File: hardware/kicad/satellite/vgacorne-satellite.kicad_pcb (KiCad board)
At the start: 2 copper layers, 134.4 x 93.5 mm, 110 parts, among them J3 SM10B-SRSS-TB, SW1 C0R0, SW10 C3R0, SW11 C3R1, SW12 C3R2, SW13 C4R0, SW14 C4R1, SW15 C4R2, SW16 C5R0, SW17 C5R1, SW18 C5R2, SW19 T0, SW2 C0R1, SW20 T1, SW21 T2, SW3 C0R2, SW4 C1R0, SW5 C1R1, SW6 C1R2, SW7 C2R0, SW8 C2R1, SW9 C2R2, U11 SN74LV4051APWR, U12 SN74LV4051APWR, U13 SN74LV4051APWR, U2 TLV75733PDBVR, U5 TLV9064IPWR, U6 SRV05-4, U7 SRV05-4

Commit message: Add trackpad, mouse column and scroll wheel; move MCU and ports
Layout
- MCU module, USB-C and trackpad move to the right half; the left half
  is now the passive satellite.
- VGA daughterboard bay moves to the inner-back corner so both cables
  leave from the back face. The bay sits 4.5 mm further back than the
  keys need, so both halves are 116 mm deep.
- Azoteq TPS65 trackpad, landscape, right beside Y/H/N under a 1 mm
  overlay. The MCU module moves to a PCB ear behind it, next to the
  VGA bay. trackpad.py selects the pad (TPS65 or 40 mm Cirque); the
  case pocket, J5 connector and QMK driver follow the selection.
- Left half: a mouse column beside T/G/B with a scroll wheel (Bourns
  PEC12R) at the top and left/right-click HE keys beside G and B.

Circuits and firmware
- Mux channels reassigned so the satellite's mouse keys and wheel fill
  its three spare channels. The wheel's A/B contacts are summed into
  four voltage levels on one channel.
- QMK: 44-key LAYOUT and a wheel decoder that feeds QMK's quadrature
  encoder driver. Trackpad on I2C1, with rules.mk now generated. The
  host test covers the wheel.
- libhmk: MS_BTN1/MS_BTN2 on the mouse keys (no encoder support).

Case and renders
- Smoother milled case: 7.25 mm walls, 25 mm minimum outside radius
  and a flat back face at the ports.
- render.py builds Blender Cycles renders from the design geometry.

Co-Authored-By: Claude Opus 5.5 (1M context) <noreply@anthropic.com>
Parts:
- added C122: 100n, Capacitor_SMD:C_0402_1005Metric, B.Cu at (133.1, 68.7)
- added C123: 100n, Capacitor_SMD:C_0402_1005Metric, B.Cu at (133.1, 87.8)
- added C222: 4.7n, Capacitor_SMD:C_0402_1005Metric, B.Cu at (138.3, 68.7)
- added C223: 4.7n, Capacitor_SMD:C_0402_1005Metric, B.Cu at (138.3, 87.8)
- added C5: 1n, Capacitor_SMD:C_0402_1005Metric, B.Cu at (143.5, 45.0)
- added ENC1: PEC12R-2217F-N0024, Rotary_Encoder:RotaryEncoder_Bourns_Horizontal_PEC12R-2x17F-Nxxxx, F.Cu at (140.0, 45.0)
- added H8: M2 standoff, vgacorne:Standoff_M2, F.Cu at (126.2, 79.0)
- added HE22: DRV5055A3QDBZR, Package_TO_SOT_SMD:SOT-23, B.Cu at (135.7, 69.5)
- added HE23: DRV5055A3QDBZR, Package_TO_SOT_SMD:SOT-23, B.Cu at (135.7, 88.6)
- added R21: 10k, Resistor_SMD:R_0402_1005Metric, B.Cu at (142.0, 45.0)
- added R22: 10k, Resistor_SMD:R_0402_1005Metric, B.Cu at (138.0, 45.3)
- added R23: 47k, Resistor_SMD:R_0402_1005Metric, B.Cu at (138.5, 43.0)
- added R24: 100k, Resistor_SMD:R_0402_1005Metric, B.Cu at (142.0, 47.3)
- added SW22: M0, vgacorne:SW_HE_MX_1u, F.Cu at (135.7, 69.5)
- added SW23: M1, vgacorne:SW_HE_MX_1u, F.Cu at (135.7, 88.6)
- moved C201 257.2 mm to (24.0, 52.1)
- moved C202 257.2 mm to (24.0, 71.1)
- moved C203 257.2 mm to (24.0, 90.2)
- moved HE1 257.2 mm to (21.4, 52.9)
- moved HE2 257.2 mm to (21.4, 71.9)
- moved HE3 257.2 mm to (21.4, 91.0)
- moved SW1 257.2 mm to (21.4, 52.9)
- moved SW2 257.2 mm to (21.4, 71.9)
- moved SW3 257.2 mm to (21.4, 91.0)
- moved C101 257.2 mm to (18.8, 52.1)
- moved C102 257.2 mm to (18.8, 71.1)
- moved C103 257.2 mm to (18.8, 90.2)
- moved H1 238.1 mm to (30.9, 62.4)
- moved H2 238.1 mm to (30.9, 81.4)
- moved HE4 219.1 mm to (40.5, 52.9)
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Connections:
- U11 pad 2: GND -> /HE_C2R0
- U11 pad 4: GND -> /HE_C2R1
- U12 pad 1: /HE_C3R1 -> /HE_C4R0
- U12 pad 12: /HE_C3R0 -> /HE_C3R2
- U12 pad 13: /HE_C2R0 -> /HE_C2R2
- U12 pad 14: /HE_C2R1 -> /HE_C3R0
- U12 pad 15: /HE_C2R2 -> /HE_C3R1
- U12 pad 2: /HE_T0 -> /HE_C4R2
- U12 pad 4: GND -> /HE_T0
- U12 pad 5: /HE_C3R2 -> /HE_C4R1
- U13 pad 1: /HE_C5R1 -> /HE_T2
- U13 pad 12: /HE_C5R0 -> /HE_T1
- U13 pad 13: /HE_C4R0 -> /HE_C5R0
- U13 pad 14: /HE_C4R1 -> /HE_C5R1
- U13 pad 15: /HE_C4R2 -> /HE_C5R2
- U13 pad 2: /HE_T1 -> /HE_M1
- U13 pad 4: /HE_T2 -> /WHEEL
- U13 pad 5: /HE_C5R2 -> /HE_M0
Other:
- board size 134.4 x 93.5 mm -> 134.4 x 93.7 mm
- board text added: "VGACorne left rev 0.1"
- board text removed: "VGACorne right rev 0.1"

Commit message: Replace the scroll wheel with a rotary encoder knob
The left half's mouse column now runs, top to bottom: right click beside
T, left click beside G, and a rotary encoder with a knob beside B, all
in line with column 5's rows.
- Encoder: Bourns PEC12R-4220F-N0024 (upright, 20 mm shaft, 24
  detents, no switch). It sits in a normal 14 mm plate cutout, which
  replaces the wheel notch. The knob is 16 mm across.
- Same readout as before: the A/B contacts are summed into four levels
  on the satellite's last spare mux channel. Nets, QMK defines and code
  are renamed from wheel to encoder (ENC, HE_ENCODER_*).
- The link connector J3 goes back to its original spot, now that the
  encoder legs are elsewhere.
- Docs, BOM, PCB images and renders regenerated.

Co-Authored-By: Claude Opus 5.5 (1M context) <noreply@anthropic.com>
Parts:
- ENC1: value PEC12R-2217F-N0024 -> PEC12R-4220F-N0024; footprint Rotary_Encoder:RotaryEncoder_Bourns_Horizontal_PEC12R-2x17F-Nxxxx -> Rotary_Encoder:RotaryEncoder_Bourns_Vertical_PEC12R-3x17F-Nxxxx
- moved C5 43.2 mm to (125.7, 84.4), turned to 180 degrees
- moved R22 42.7 mm to (126.2, 86.3)
- moved ENC1 42.7 mm to (128.2, 86.1)
- moved R21 42.7 mm to (130.2, 86.1)
- moved R24 42.7 mm to (130.2, 88.3)
- moved R23 42.3 mm to (128.3, 84.1)
- moved C123 38.1 mm to (133.1, 49.7)
- moved C223 38.1 mm to (138.3, 49.7)
- moved HE23 38.1 mm to (135.7, 50.5)
- moved SW23 38.1 mm to (135.7, 50.5)
- moved C4 10.2 mm to (132.6, 56.9)
- moved C2 6.31 mm to (129.1, 54.3)
- moved U6 5.93 mm to (139.0, 44.5), turned to 90 degrees
- moved C1 5.42 mm to (129.1, 56.2), turned to 0 degrees
- moved U5 5.17 mm to (137.6, 57.3), turned to 0 degrees
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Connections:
- net /WHEEL renamed /ENC
- net /WHEEL_A renamed /ENC_A
- net /WHEEL_B renamed /ENC_B

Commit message: Fix design audit findings
Electrical:
- Re-map the castellated module's pads so neighbours on each edge follow
  the LQFP: USB D+/D- together between grounds at the corner nearest the
  USB-C, the six ADC inputs grouped beside +3.3VA, a ground away from the
  select lines.
- Put 1k between each DRV5055 output and its 4.7n cap (TI: no capacitor
  straight on the output).
- STM32F446 module: pull PB2/BOOT1 down so BOOT reaches DFU; pull PA10 up.
- Replace the XC6206 with a second TLV75733, and the link polyfuse with a
  TPS2051C switch (soft start, current limit) so hot-plugging the satellite
  can't brown out the MCU. F1 is now 750 mA.
- USB net class 0.4/0.15 mm: ~97 ohm differential against the pour on both
  2-layer boards (was ~120).
- BOM gains a Tolerance column; part numbers for the F446 crystal.

Mechanical:
- Case foam 2 mm, leaving 0.5 mm under the bottom-side parts (the old stack
  pressed the foam into every sensor).
- USB-C overhangs the ear by 0.46 mm and the opening takes a spec-maximum
  overmould (13.95 x 8.1 mm); the old 11 x 6 mm stopped most plugs short.
- DE-15 rear-mount cutout 20.5 x 11.4 mm; floor pockets under the USB-C and
  encoder pins; plate foam clears the module and the encoder's pins.
- Knob 11.5 mm tall so it clears the encoder's collar.

Docs, PCB images and renders updated to match.

Co-Authored-By: Claude Opus 5.5 (1M context) <noreply@anthropic.com>
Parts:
- added R301: 1k, Resistor_SMD:R_0402_1005Metric, B.Cu at (24.0, 54.2)
- added R302: 1k, Resistor_SMD:R_0402_1005Metric, B.Cu at (24.0, 73.3)
- added R303: 1k, Resistor_SMD:R_0402_1005Metric, B.Cu at (24.0, 92.3)
- added R304: 1k, Resistor_SMD:R_0402_1005Metric, B.Cu at (43.1, 54.2)
- added R305: 1k, Resistor_SMD:R_0402_1005Metric, B.Cu at (43.1, 73.3)
- added R306: 1k, Resistor_SMD:R_0402_1005Metric, B.Cu at (43.1, 92.3)
- added R307: 1k, Resistor_SMD:R_0402_1005Metric, B.Cu at (62.1, 49.4)
- added R308: 1k, Resistor_SMD:R_0402_1005Metric, B.Cu at (62.1, 68.5)
- added R309: 1k, Resistor_SMD:R_0402_1005Metric, B.Cu at (62.1, 87.5)
- added R310: 1k, Resistor_SMD:R_0402_1005Metric, B.Cu at (81.2, 47.1)
- added R311: 1k, Resistor_SMD:R_0402_1005Metric, B.Cu at (81.2, 66.1)
- added R312: 1k, Resistor_SMD:R_0402_1005Metric, B.Cu at (81.2, 85.2)
- added R313: 1k, Resistor_SMD:R_0402_1005Metric, B.Cu at (100.2, 49.4)
- added R314: 1k, Resistor_SMD:R_0402_1005Metric, B.Cu at (100.2, 68.5)
- added R315: 1k, Resistor_SMD:R_0402_1005Metric, B.Cu at (100.2, 87.5)
- added R316: 1k, Resistor_SMD:R_0402_1005Metric, B.Cu at (119.3, 51.8)
- added R317: 1k, Resistor_SMD:R_0402_1005Metric, B.Cu at (119.3, 70.9)
- added R318: 1k, Resistor_SMD:R_0402_1005Metric, B.Cu at (119.3, 89.9)
- added R319: 1k, Resistor_SMD:R_0402_1005Metric, B.Cu at (90.7, 109.0)
- added R320: 1k, Resistor_SMD:R_0402_1005Metric, B.Cu at (111.2, 111.7)
- added R321: 1k, Resistor_SMD:R_0402_1005Metric, B.Cu at (133.0, 110.1)
- added R322: 1k, Resistor_SMD:R_0402_1005Metric, B.Cu at (138.3, 70.9)
- added R323: 1k, Resistor_SMD:R_0402_1005Metric, B.Cu at (138.3, 51.8)
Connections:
- HE1 pad 2: /HE_C0R0 -> /HE_C0R0_OUT
- HE10 pad 2: /HE_C3R0 -> /HE_C3R0_OUT
- HE11 pad 2: /HE_C3R1 -> /HE_C3R1_OUT
- HE12 pad 2: /HE_C3R2 -> /HE_C3R2_OUT
- HE13 pad 2: /HE_C4R0 -> /HE_C4R0_OUT
- HE14 pad 2: /HE_C4R1 -> /HE_C4R1_OUT
- HE15 pad 2: /HE_C4R2 -> /HE_C4R2_OUT
- HE16 pad 2: /HE_C5R0 -> /HE_C5R0_OUT
- HE17 pad 2: /HE_C5R1 -> /HE_C5R1_OUT
- HE18 pad 2: /HE_C5R2 -> /HE_C5R2_OUT
- HE19 pad 2: /HE_T0 -> /HE_T0_OUT
- HE2 pad 2: /HE_C0R1 -> /HE_C0R1_OUT
- HE20 pad 2: /HE_T1 -> /HE_T1_OUT
- HE21 pad 2: /HE_T2 -> /HE_T2_OUT
- HE22 pad 2: /HE_M0 -> /HE_M0_OUT
- HE23 pad 2: /HE_M1 -> /HE_M1_OUT
- HE3 pad 2: /HE_C0R2 -> /HE_C0R2_OUT
- HE4 pad 2: /HE_C1R0 -> /HE_C1R0_OUT
- HE5 pad 2: /HE_C1R1 -> /HE_C1R1_OUT
- HE6 pad 2: /HE_C1R2 -> /HE_C1R2_OUT
- HE7 pad 2: /HE_C2R0 -> /HE_C2R0_OUT
- HE8 pad 2: /HE_C2R1 -> /HE_C2R1_OUT
- HE9 pad 2: /HE_C2R2 -> /HE_C2R2_OUT

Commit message: Route the VGA daughterboard with Freerouting
hardware/route.py drives Freerouting directly (the KiCad MCP's autorouter
trips over a pcbnew/Python 3.14 binding bug): signals first with the
ground pours as planes, then ground as tracks round the locked signals,
then the pours and ground stitching vias. The daughterboard routes
completely and passes DRC.

To make it routable:
- the 10-pin link order now follows the DE-15 under the pigtail pads
  (J3 on both halves follows; the pigtail stays 1:1, +5 V on pin 1);
- the pigtail pads are shorter and at the board edge, leaving a via
  channel above the connector;
- the socket keeps KiCad's 1.6 mm pads round Amphenol's 1.2 mm holes,
  so a track fits between pins;
- both cable-variant jumpers sit together by pins 9 and 15.

generate.py --force pcbs now leaves boards with tracks alone.

Co-Authored-By: Claude Opus 5.5 (1M context) <noreply@anthropic.com>
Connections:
- J3 pad 10: /LINK_C -> GND
- J3 pad 2: GND -> /LINK_DET
- J3 pad 3: /LINK_S0 -> /LINK_S1
- J3 pad 4: /LINK_S1 -> /LINK_S0
- J3 pad 6: /LINK_DET -> /LINK_C
- J3 pad 7: GND -> /LINK_B
- J3 pad 9: /LINK_B -> GND

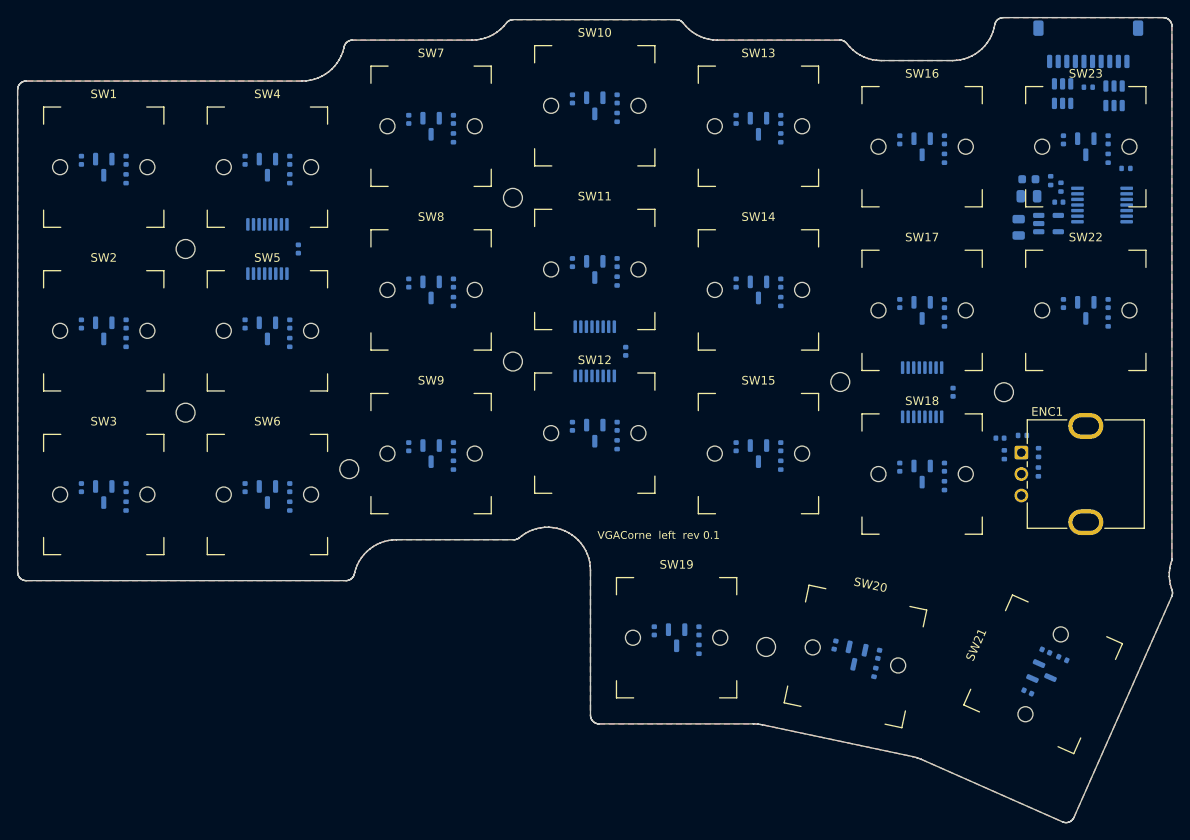
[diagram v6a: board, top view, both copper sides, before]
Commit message: Route the satellite and most of the main board
route.py now runs its strategies in parallel and keeps the first that
connects everything, streams Freerouting's logs to route-logs/, drops stray
vias, adds a finishing pass on boards left with gaps, and stitches ground
every 5 mm on large boards (2.5 mm on small ones).

The satellite is fully routed. On the main board the regulators moved to
the USB-C ear and the remote ADC resistors to the module's ADC pads, which
took the unconnected count from 9 to 3. The Power class is 0.3 mm so
tracks can enter 0.5 mm-pitch pads.

The main board is not finished: LINK_B (J3.7-U7.3), VBUS at USB-C A4 and
LINK_A at R8.1 are still open, C18's ground pad has no via to the pour
(starved thermal, so `generate.py check` fails), and the USB pair needs
rerouting as a coupled pair. docs/bring-up.md lists the steps.

Co-Authored-By: Claude Opus 5.5 (1M context) <noreply@anthropic.com>
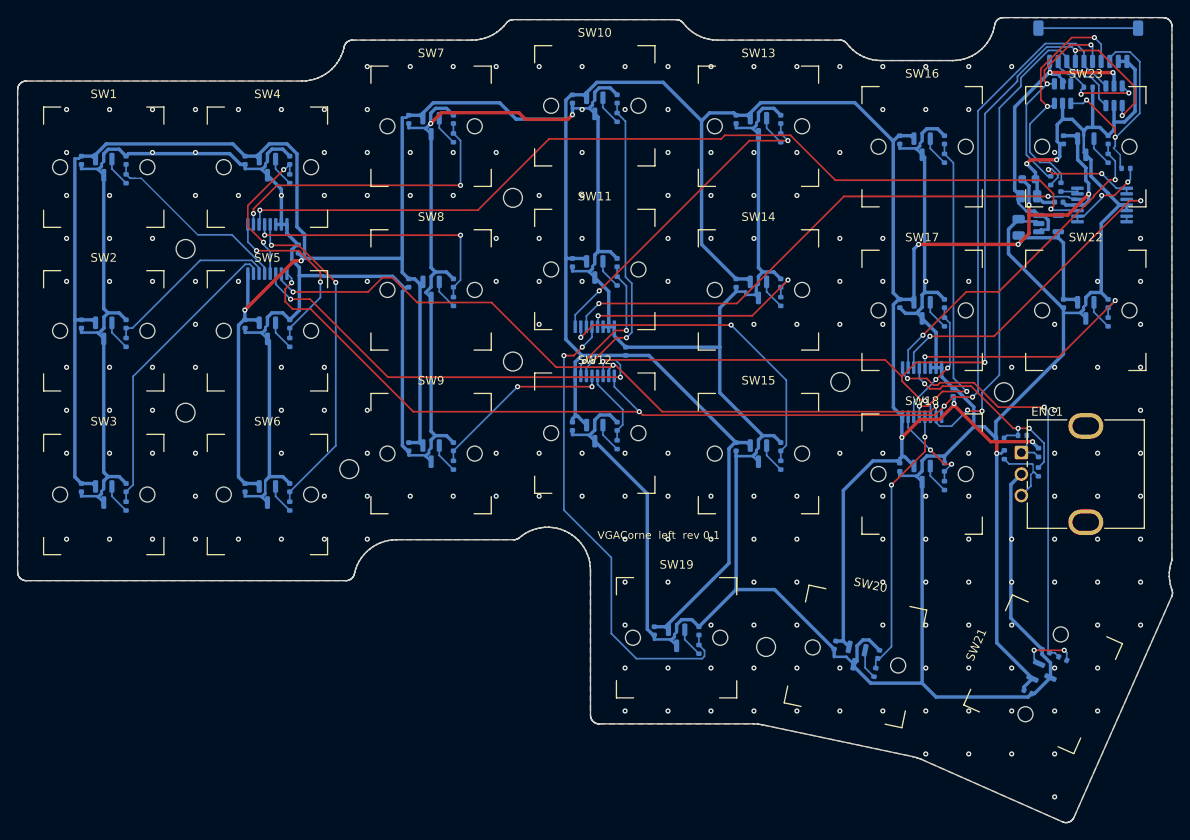
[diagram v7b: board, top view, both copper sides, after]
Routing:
- net GND: track 0.00 -> 699.6 mm, vias 0 -> 223
- net +3.3VA: track 0.00 -> 546.6 mm, vias 0 -> 10
- net /LINK_S0: track 0.00 -> 161.9 mm, vias 0 -> 7
- net /LINK_S2: track 0.00 -> 151.6 mm, vias 0 -> 4
- net /LINK_S1: track 0.00 -> 150.9 mm, vias 0 -> 5
- net /MUX_A: track 0.00 -> 105.5 mm, vias 0 -> 2
- net /MUX_B: track 0.00 -> 64.3 mm, vias 0 -> 2
- net /HE_T0: track 0.00 -> 54.9 mm, vias 0 -> 2
- net /HE_T2: track 0.00 -> 49.1 mm, vias 0 -> 2
- net /HE_C1R2: track 0.00 -> 39.5 mm, vias 0 -> 2
- net /HE_M1: track 0.00 -> 38.9 mm, vias 0 -> 2
- net /HE_C4R2: track 0.00 -> 38.1 mm, vias 0 -> 2
- net /HE_C5R0: track 0.00 -> 37.4 mm, vias 0 -> 2
- net /MUX_C: track 0.00 -> 37.2 mm, vias 0 -> 2
- net /HE_C4R0: track 0.00 -> 36.9 mm, vias 0 -> 2
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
